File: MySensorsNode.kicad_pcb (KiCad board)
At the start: 2 copper layers, 50 x 50 mm, 60 parts, among them P1 MYSX_1.5, P2 CONN_02X03, P3 CONN_01X03, P4 CONN_01X03, Q1 DMP3056L-7, Q2 DMP3056L-7, U1 LD1117DT33TR, U2 TPS61097A, U3 ATSHA204A, U4 RFM69HW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

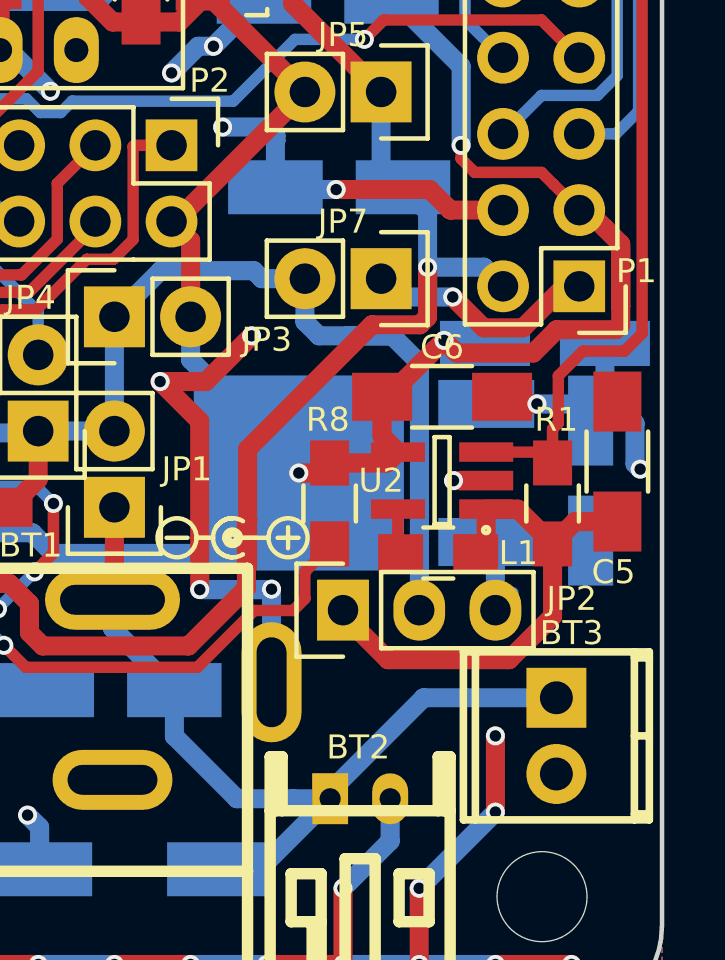
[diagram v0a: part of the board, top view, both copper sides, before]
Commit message: Added a step-up reg and some sourcing details
Added TI TPS61221 (3.3V fixed) as an alternative to TPS61097A.
Also added some more sourcing details to some components in the
schematic.
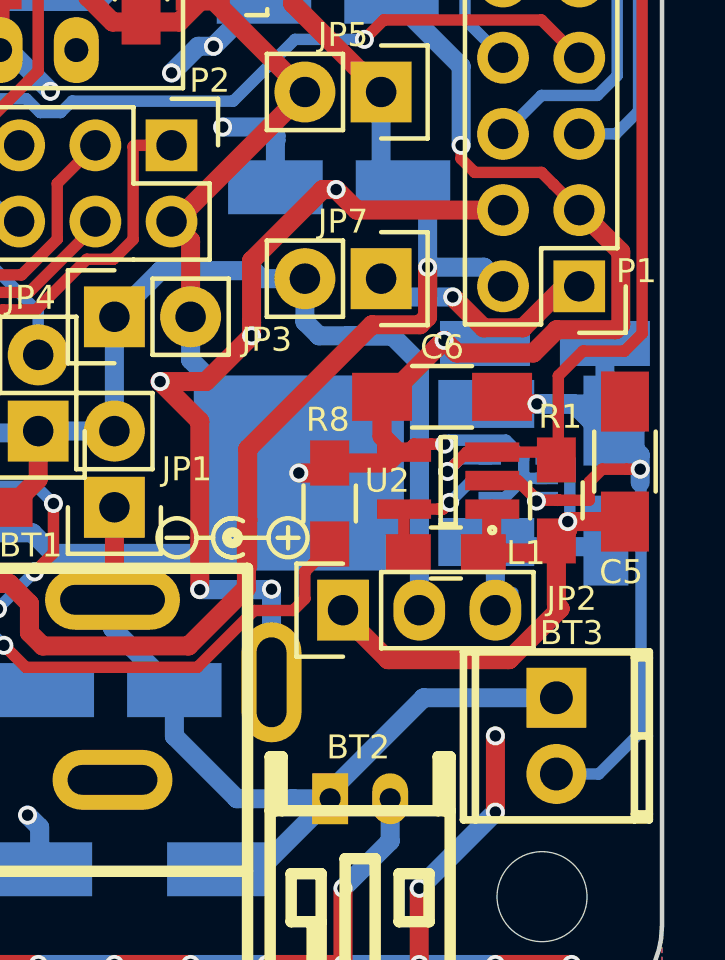
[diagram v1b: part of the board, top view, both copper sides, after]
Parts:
- added U9: TPS6122X, Housings_SOT-23_SOT-143_TSOT-6:SC-70-6, B.Cu at (181.5, 105.4)
- moved C4 0.51 mm to (184.4, 105.5)
- moved C5 0.25 mm to (185.0, 104.9)
- moved L1 0.25 mm to (179.1, 107.9)
- moved U2 0.20 mm to (179.1, 105.5)
- moved R1 0.16 mm to (182.8, 106.2)
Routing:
- net GND: track 396.0 -> 425.4 mm
- net +3V3: track 200.9 -> 206.4 mm, vias 8 -> 9
- net Net-(C5-Pad1): track 17.5 -> 21.5 mm, vias 0 -> 1
- net Net-(JP6-Pad2): track 33.1 -> 36.5 mm, vias 0 -> 1
- net Net-(L1-Pad1): track 1.50 -> 4.76 mm, vias 0 -> 1
- net Net-(C4-Pad1): track 6.72 -> 7.36 mm

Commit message: Updated CR123 battery holder footprint
Fixes #11
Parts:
- U9: value TPS6122X -> TPS61221
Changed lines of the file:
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@@
-(kicad_pcb (version 4) (host pcbnew "(2015-07-30 BZR 6023, Git cb629e0)-product")
+(kicad_pcb (version 4) (host pcbnew 0.201509101502+6177~30~ubuntu14.04.1-product)
   (general
     (links 181)
     (no_connects 0)
-    (area 136.195999 73.304999 186.350001 123.455601)
+    (area 128.621001 70.8806 190.768246 125.35946)
     (thickness 1.2)
     (drawings 22)
@@
       (effects (font (size 0.8 0.8) (thickness 0.16)) (justify mirror))
     )
-    (fp_text value TPS6122X (at 0.04064 -4.191 270) (layer B.Fab)
+    (fp_text value TPS61221 (at 0.04064 -4.191 270) (layer B.Fab)
       (effects (font (size 1 1) (thickness 0.15)) (justify mirror))
     )

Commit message: Minor layout beautifications
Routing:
- net GND: track 425.4 -> 399.6 mm, vias 185 -> 167
- net (no net): track 0.00 -> 2.54 mm, vias 0 -> 3
